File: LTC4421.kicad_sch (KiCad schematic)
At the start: 59 parts, among them U2 LTC4421CG-PBF, U3 74LVC2G07GV,125, U4 74LVC2G07GV,125, U5 74LVC2G07GV,125

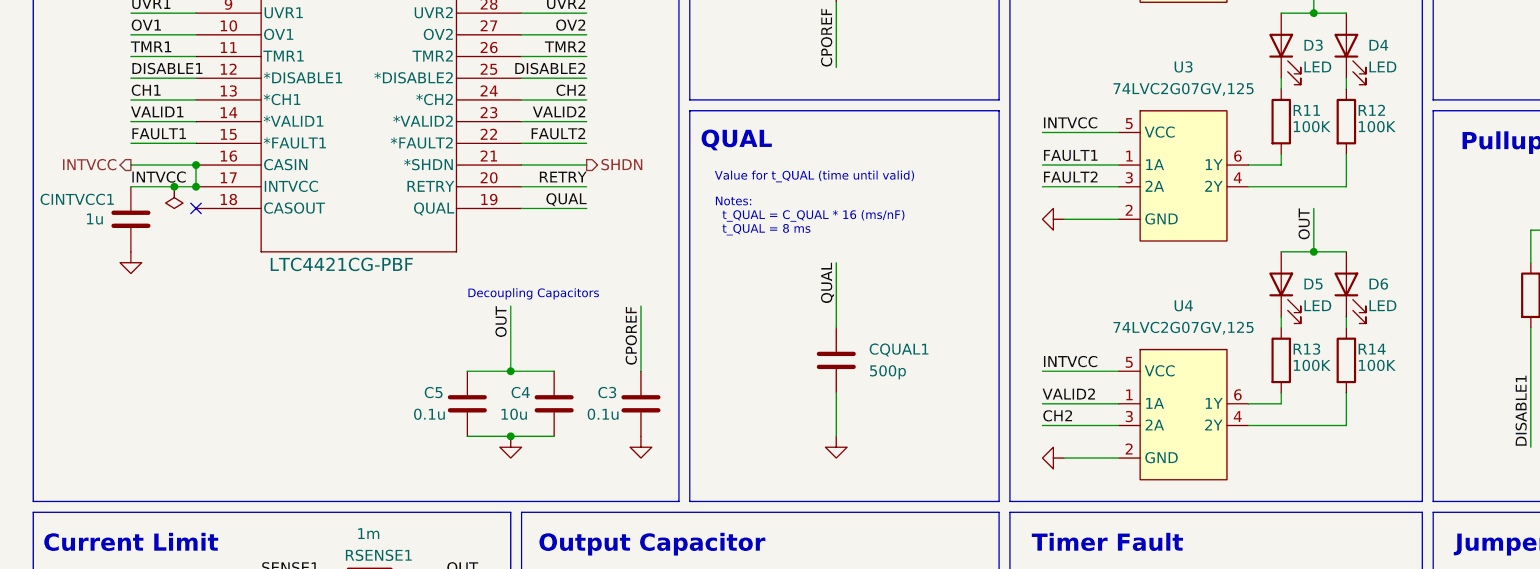
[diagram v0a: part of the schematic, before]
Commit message: SHDN, non-crit, and ignition sequence fixes
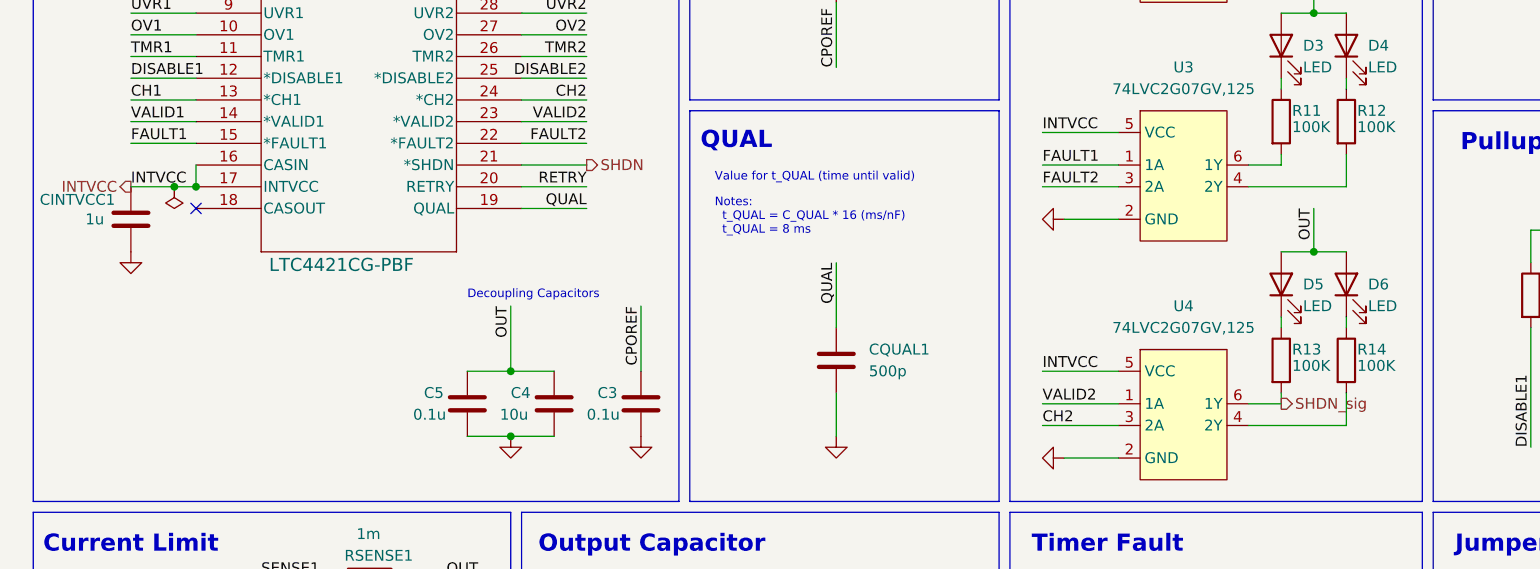
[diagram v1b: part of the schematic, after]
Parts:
- JP1, JP2, JP3: footprint Connector_PinHeader_1.00mm:PinHeader_1x03_P1.00mm_Vertical -> Connector_PinHeader_2.54mm:PinHeader_1x03_P2.54mm_Vertical
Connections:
- net SHDN_sig: now reaches R13.2, U4.6 (1Y)
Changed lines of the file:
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@@
 	)
 	(junction
-		(at 31.75 66.04)
-		(diameter 0)
-		(color 0 0 0 0)
-	)
-	(junction
 		(at 223.52 73.66)
 		(diameter 0)
@@
 	(wire
 		(pts
-			(xy 24.13 66.04) (xy 31.75 66.04)
-		)
-		(stroke
-			(width 0)
-			(type default)
-		)
-	)
-	(wire
-		(pts
 			(xy 270.51 148.59) (xy 270.51 160.02)
 		)
@@
 	(hierarchical_label "INTVCC"
 		(shape output)
-		(at 24.13 66.04 180)
+		(at 24.13 68.58 180)
 		(fields_autoplaced yes)
 		(effects
@@
 		)
 	)
+	(hierarchical_label "SHDN_sig"
+		(shape output)
+		(at 158.75 93.98 0)
+		(fields_autoplaced yes)
+		(effects
+			(font
+				(size 1.27 1.27)
+			)
+			(justify left)
+		)
+	)
 	(hierarchical_label "SOURCE1"
 		(shape input)
@@
 			)
 		)
-		(property "Footprint" "Connector_PinHeader_1.00mm:PinHeader_1x03_P1.00mm_Vertical"
+		(property "Footprint" "Connector_PinHeader_2.54mm:PinHeader_1x03_P2.54mm_Vertical"
 			(at 194.31 121.92 0)
 			(effects
@@
 			)
 		)
-		(property "Footprint" "Connector_PinHeader_1.00mm:PinHeader_1x03_P1.00mm_Vertical"
+		(property "Footprint" "Connector_PinHeader_2.54mm:PinHeader_1x03_P2.54mm_Vertical"
 			(at 261.62 121.92 0)
 			(effects
@@
 			)
 		)
-		(property "Footprint" "Connector_PinHeader_1.00mm:PinHeader_1x03_P1.00mm_Vertical"
+		(property "Footprint" "Connector_PinHeader_2.54mm:PinHeader_1x03_P2.54mm_Vertical"
 			(at 228.6 121.92 0)
 			(effects

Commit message: bruh changes
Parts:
- removed D3, D4: LED, LED_SMD:LED_0805_2012Metric, symbol Device:LED
- removed R11, R12: 100K, Resistor_SMD:R_0805_2012Metric, symbol Device:R
- removed U3: 74LVC2G07GV,125, Package_TO_SOT_SMD:ROHM_SOT-457_ClockwisePinNumbering, symbol PowerBoardLib:74LVC2G07GV,125
- U4, U5: footprint Package_TO_SOT_SMD:ROHM_SOT-457_ClockwisePinNumbering -> Package_TO_SOT_SMD:SC-74-6_1.55x2.9mm_P0.95mm
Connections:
- net CH1: now also U5.3 (2A); no longer U5.1 (1A)
- net CH2: now also U4.1 (1A); no longer U4.3 (2A)
- net Non-Crit Drive: now also U5.4 (2Y); no longer U5.6 (1Y)
- net SHDN_sig: now also U4.4 (2Y); no longer U4.6 (1Y)
- net VALID1: now also U5.1 (1A); no longer U5.3 (2A)
- net VALID2: now also U4.3 (2A); no longer U4.1 (1A)
- net at R16.2: now also U5.6 (1Y); no longer U5.4 (2Y)
- net at R14.2: now also U4.6 (1Y); no longer U4.4 (2Y)
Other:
- moved on the sheet: D5, D6, D7, D8, R13, R14, R15, R16

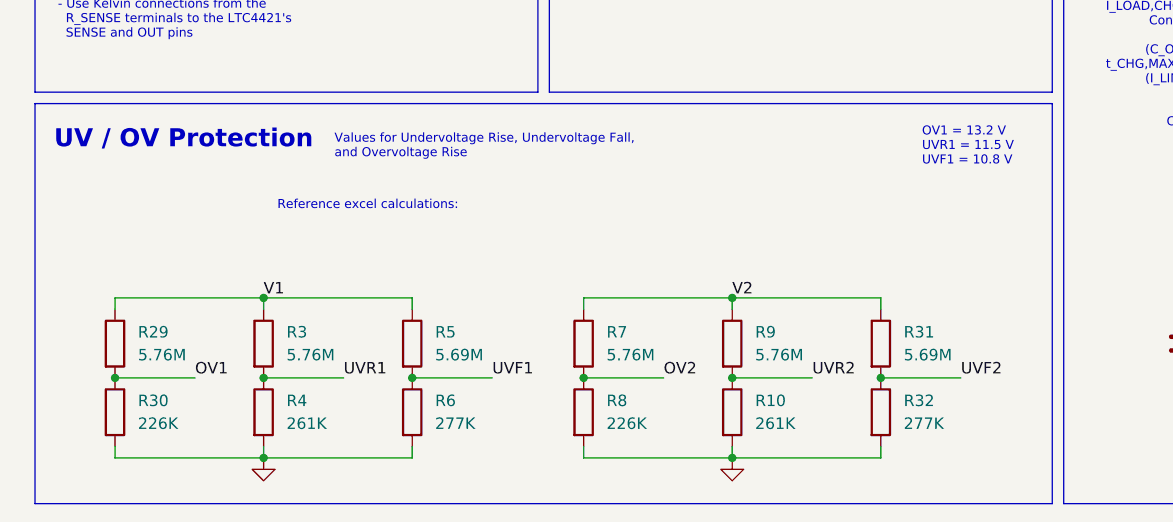
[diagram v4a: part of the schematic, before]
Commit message: changed UV and OV resistor circuit
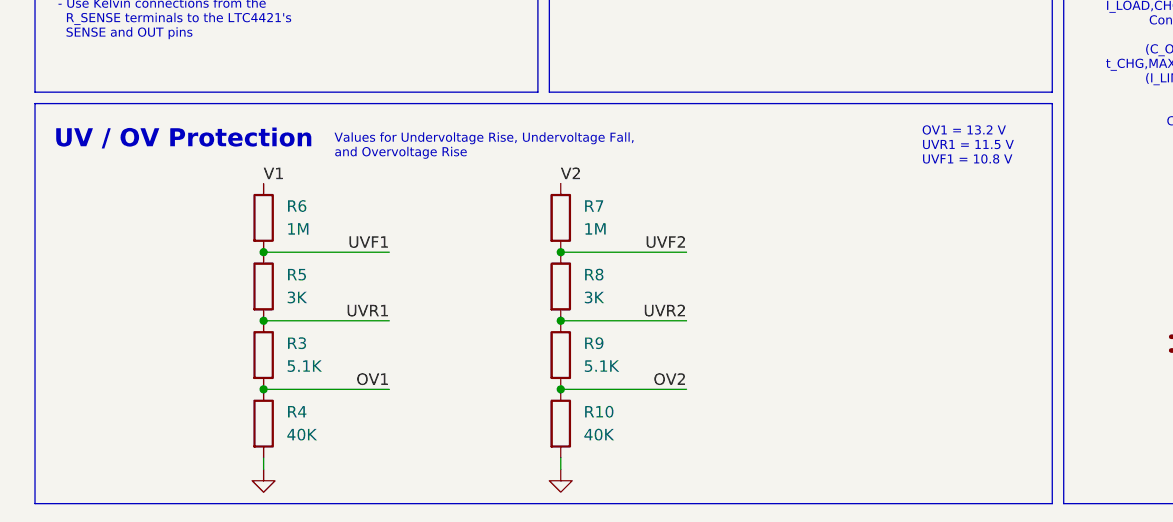
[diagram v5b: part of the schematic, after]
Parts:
- removed R29: 5.76M, Resistor_SMD:R_0805_2012Metric, symbol Device:R
- removed R30: 226K, Resistor_SMD:R_0805_2012Metric, symbol Device:R
- removed R31: 5.69M, Resistor_SMD:R_0805_2012Metric, symbol Device:R
- removed R32: 277K, Resistor_SMD:R_0805_2012Metric, symbol Device:R
- R10, R4: value 261K -> 40K
- R3, R9: value 5.76M -> 5.1K
- R5: value 5.69M -> 3K
- R6: value 277K -> 1M; MFG PN CRCW0805287KFKEA -> RC0805FR-075M76L
- R7: value 5.76M -> 1M
- R8: value 226K -> 3K; MFG PN RC0805FR-07215KL -> RC0805FR-075M76L
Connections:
- net GND: no longer R6.2, R8.2
- net OV1: now also R3.2, R4.1
- net OV2: now also R10.1, R9.2; no longer R7.2, R8.1
- net UVF1: now also R5.1, R6.2; no longer R5.2, R6.1
- net UVF2: now also R7.2, R8.1
- net UVR1: now also R3.1, R5.2; no longer R3.2, R4.1
- net UVR2: now also R8.2, R9.1; no longer R10.1, R9.2
- net V1: now also R6.1; no longer R3.1, R5.1
- net V2: no longer R9.1
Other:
- note removed: "Reference excel calculations:"
- moved on the sheet: R3, R4

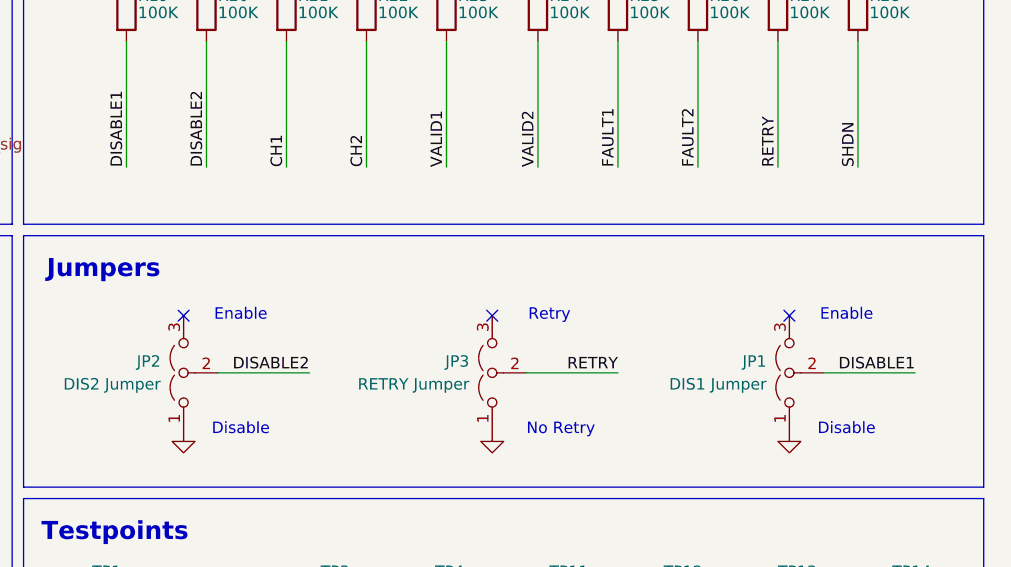
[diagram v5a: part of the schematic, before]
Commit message: added auto-retry functionality
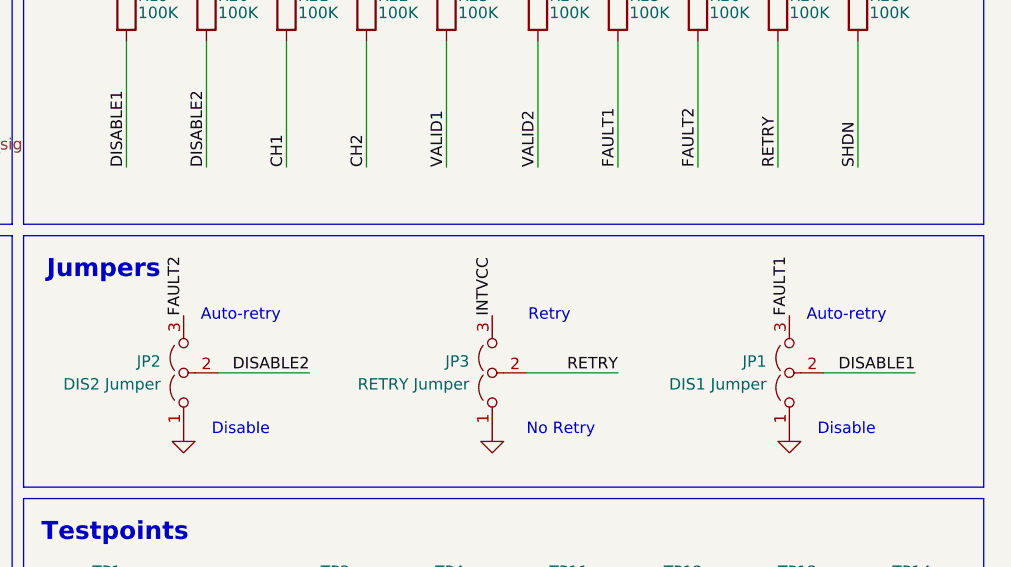
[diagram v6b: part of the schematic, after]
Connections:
- net FAULT1: now also JP1.3 (B)
- net FAULT2: now also JP2.3 (B)
- net INTVCC: now also JP3.3 (B)
- no-connect marks 4 -> 1
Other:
- note added: "Auto-retry"
- note removed: "Enable"
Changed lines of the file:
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@@
 		)
 	)
-	(text "Enable"
+	(text "Auto-retry\n"
 		(exclude_from_sim no)
 		(at 200.66 115.57 0)
@@
 		)
 	)
-	(text "Enable"
+	(text "Auto-retry"
 		(exclude_from_sim no)
 		(at 267.97 115.57 0)
@@
 		(at 31.75 71.12)
 	)
-	(no_connect
-		(at 228.6 115.57)
-	)
-	(no_connect
-		(at 261.62 115.57)
-	)
-	(no_connect
-		(at 194.31 115.57)
-	)
 	(wire
 		(pts
@@
 	)
 	(label "INTVCC"
+		(at 228.6 115.57 90)
+		(effects
+			(font
+				(size 1.27 1.27)
+			)
+			(justify left bottom)
+		)
+	)
+	(label "INTVCC"
 		(at 24.13 68.58 0)
 		(effects
@@
 		)
 	)
+	(label "FAULT2"
+		(at 194.31 115.57 90)
+		(effects
+			(font
+				(size 1.27 1.27)
+			)
+			(justify left bottom)
+		)
+	)
 	(label "CH1"
 		(at 205.74 99.06 90)
@@
 		)
 	)
+	(label "FAULT1"
+		(at 261.62 115.57 90)
+		(effects
+			(font
+				(size 1.27 1.27)
+			)
+			(justify left bottom)
+		)
+	)

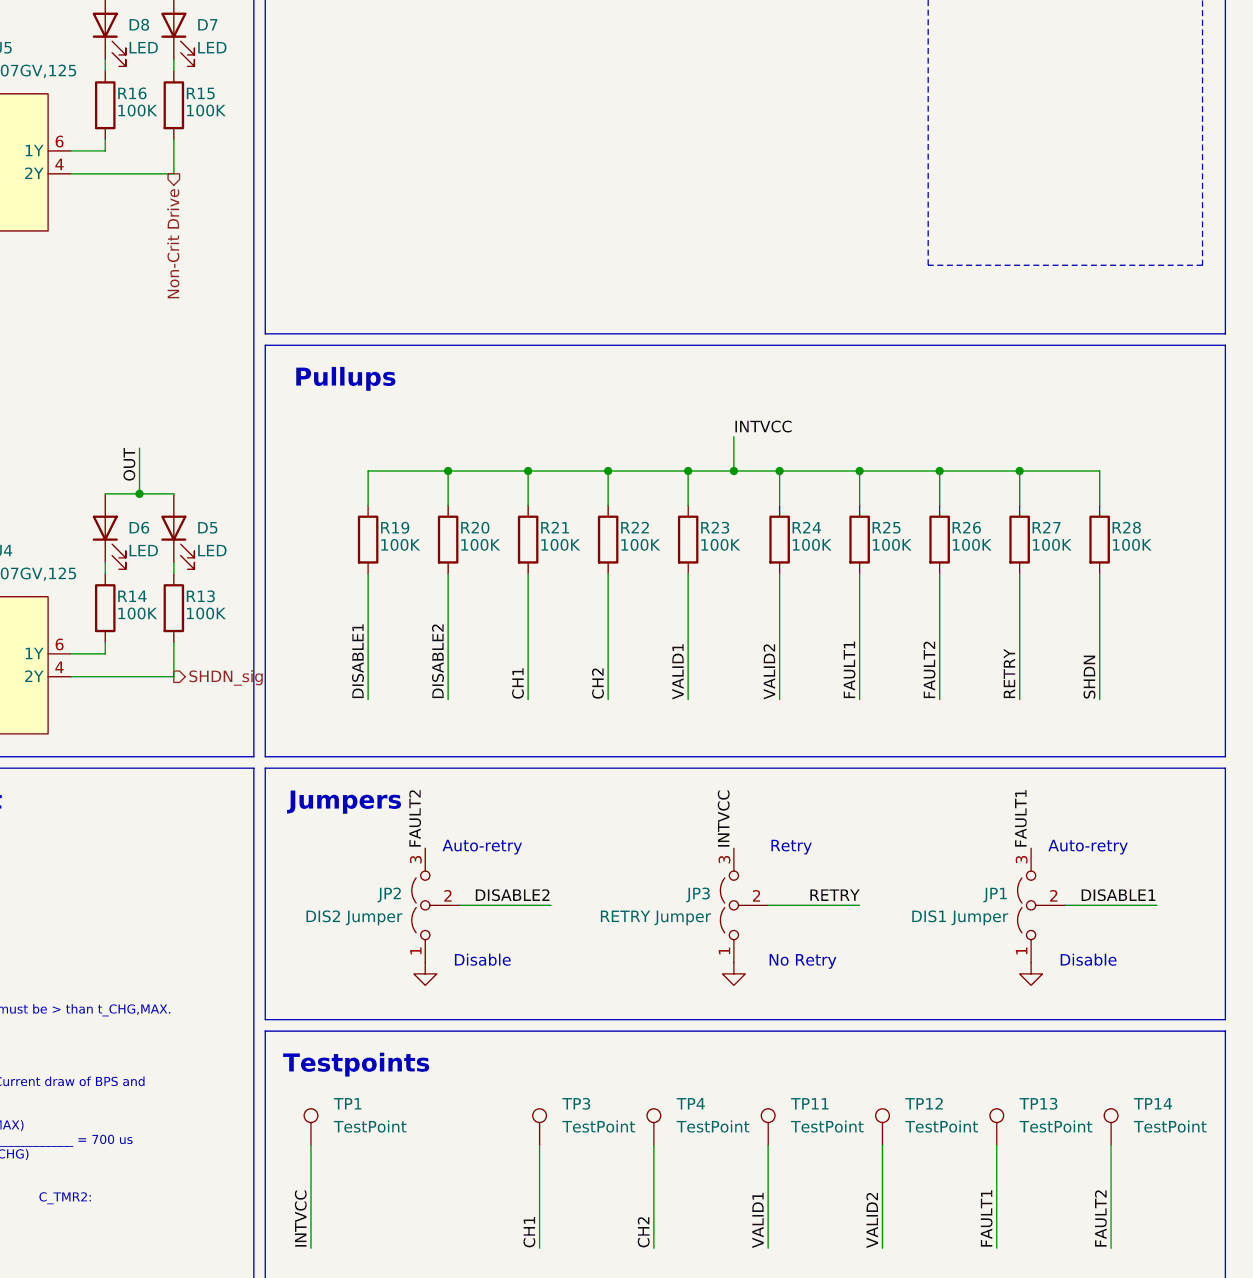
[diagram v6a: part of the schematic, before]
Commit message: added testpoints for shdn sig and non-crit enable
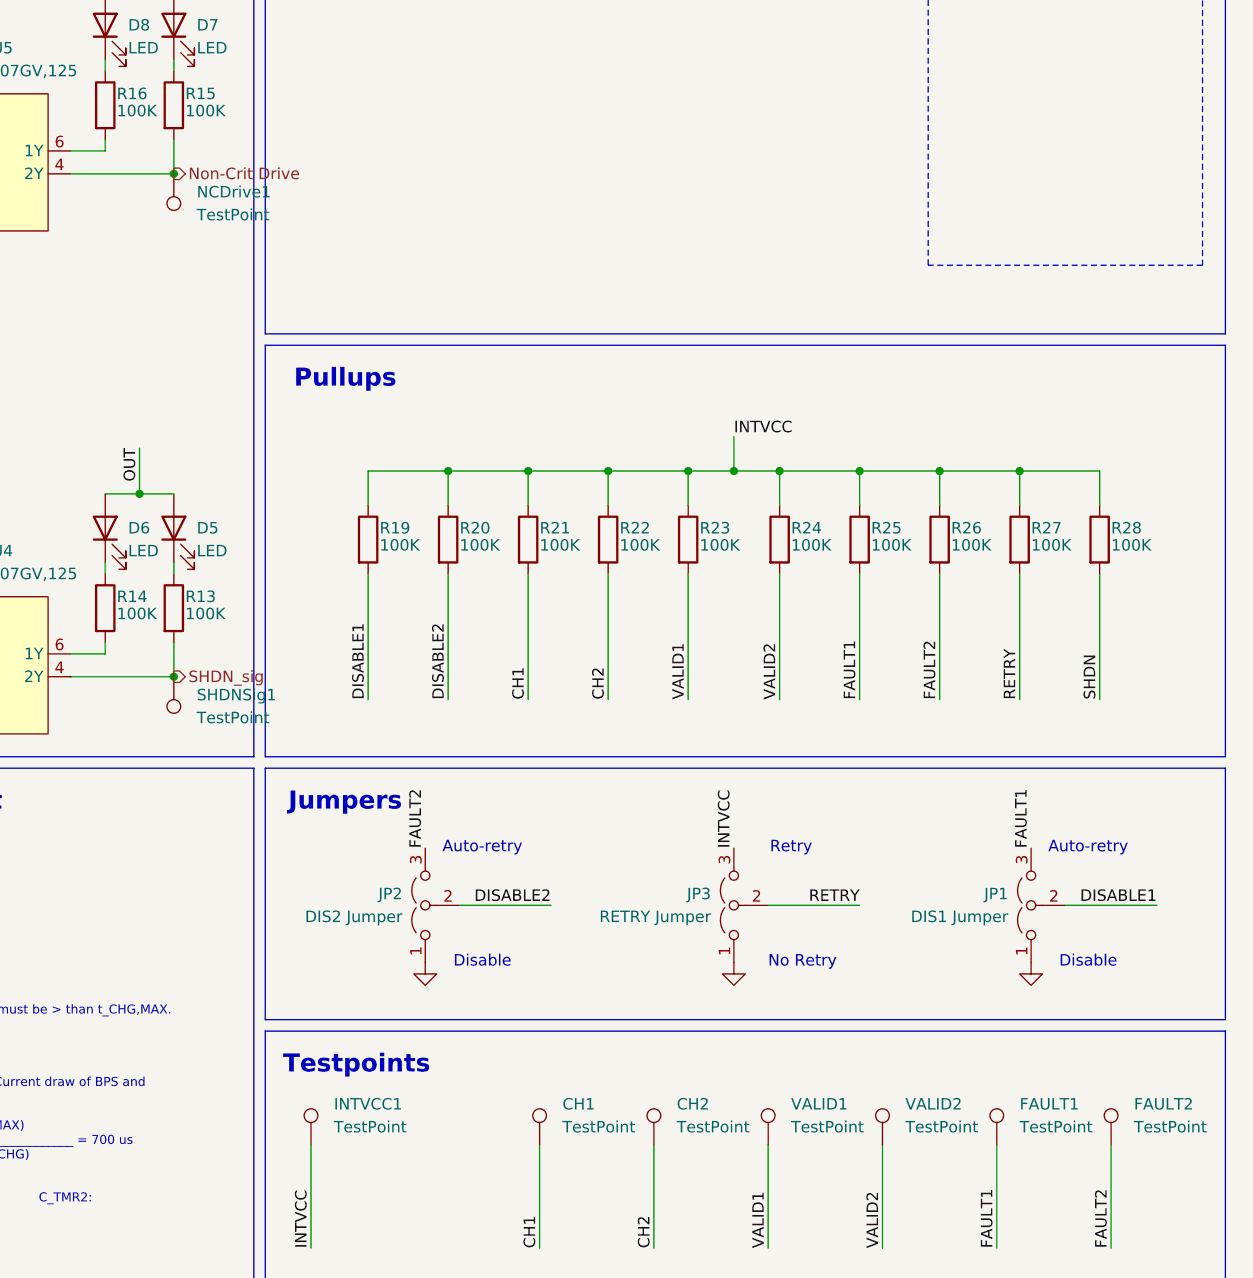
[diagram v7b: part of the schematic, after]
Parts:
- added NCDrive1, SHDNSig1: TestPoint, TestPoint:TestPoint_Pad_D2.0mm, symbol Connector:TestPoint
- renumbered TP3 to CH1, TP4 to CH2, TP13 to FAULT1, TP14 to FAULT2, TP1 to INTVCC1, TP11 to VALID1, TP12 to VALID2
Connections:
- net Non-Crit Drive: now also NCDrive1.1
- net SHDN_sig: now also SHDNSig1.1

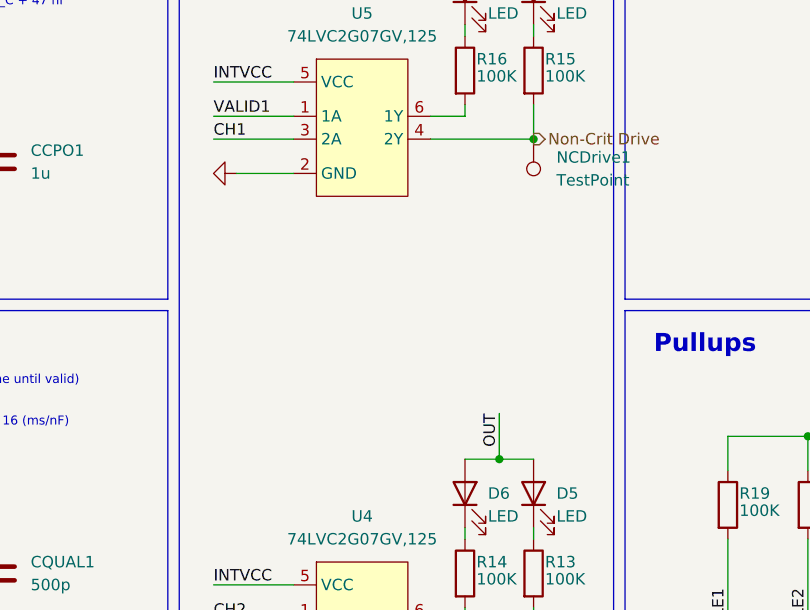
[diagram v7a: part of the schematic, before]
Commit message: added fault LEDs
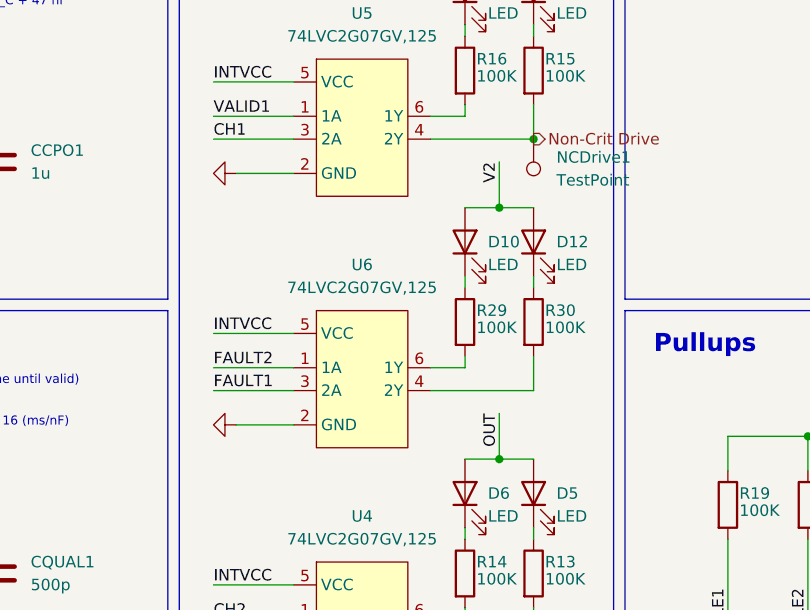
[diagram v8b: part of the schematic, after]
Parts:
- added D10, D12: LED, LED_SMD:LED_0805_2012Metric, symbol Device:LED
- added R29, R30: 100K, Resistor_SMD:R_0805_2012Metric, symbol Device:R
- added U6: 74LVC2G07GV,125, Package_TO_SOT_SMD:SC-74-6_1.55x2.9mm_P0.95mm, symbol PowerBoardLib:74LVC2G07GV,125
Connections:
- net FAULT1: now also U6.3 (2A)
- net FAULT2: now also U6.1 (1A)
- net GND: now also U6.2 (GND)
- net INTVCC: now also U6.5 (VCC)
- net V2: now also D10.2 (A), D12.2 (A)
- new net: R30.2, U6.4 (2Y)
- new net: R29.2, U6.6 (1Y)
- new net: D12.1 (K), R30.1
- new net: D10.1 (K), R29.1
